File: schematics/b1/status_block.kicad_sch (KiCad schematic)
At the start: 42 parts, among them Q1 2N3904, Q2 2N3904, Q3 2N3904, Q4 2N3904, Q5 2N3904, Q6 2N3904, Q7 2N3904, Q8 2N3904, Q9 2N3904, SW9 SW_SPDT, U2 74HC595, U3 NE555P

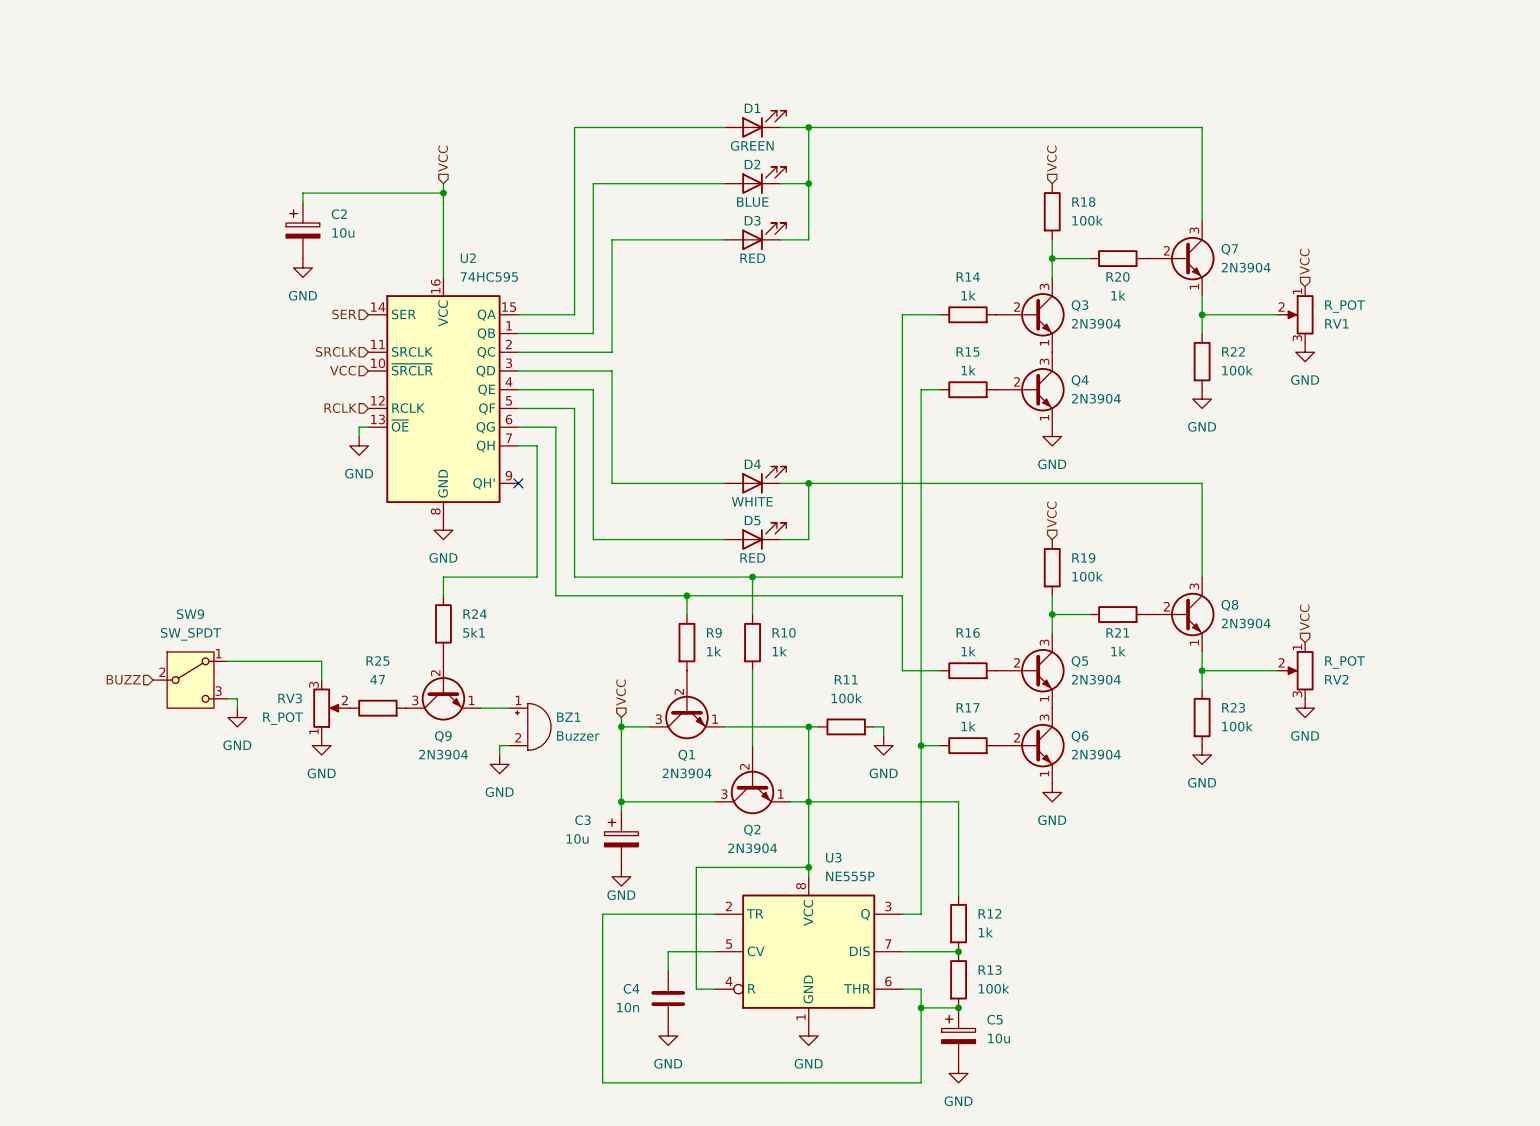
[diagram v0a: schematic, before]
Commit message: Added status block to the index page.
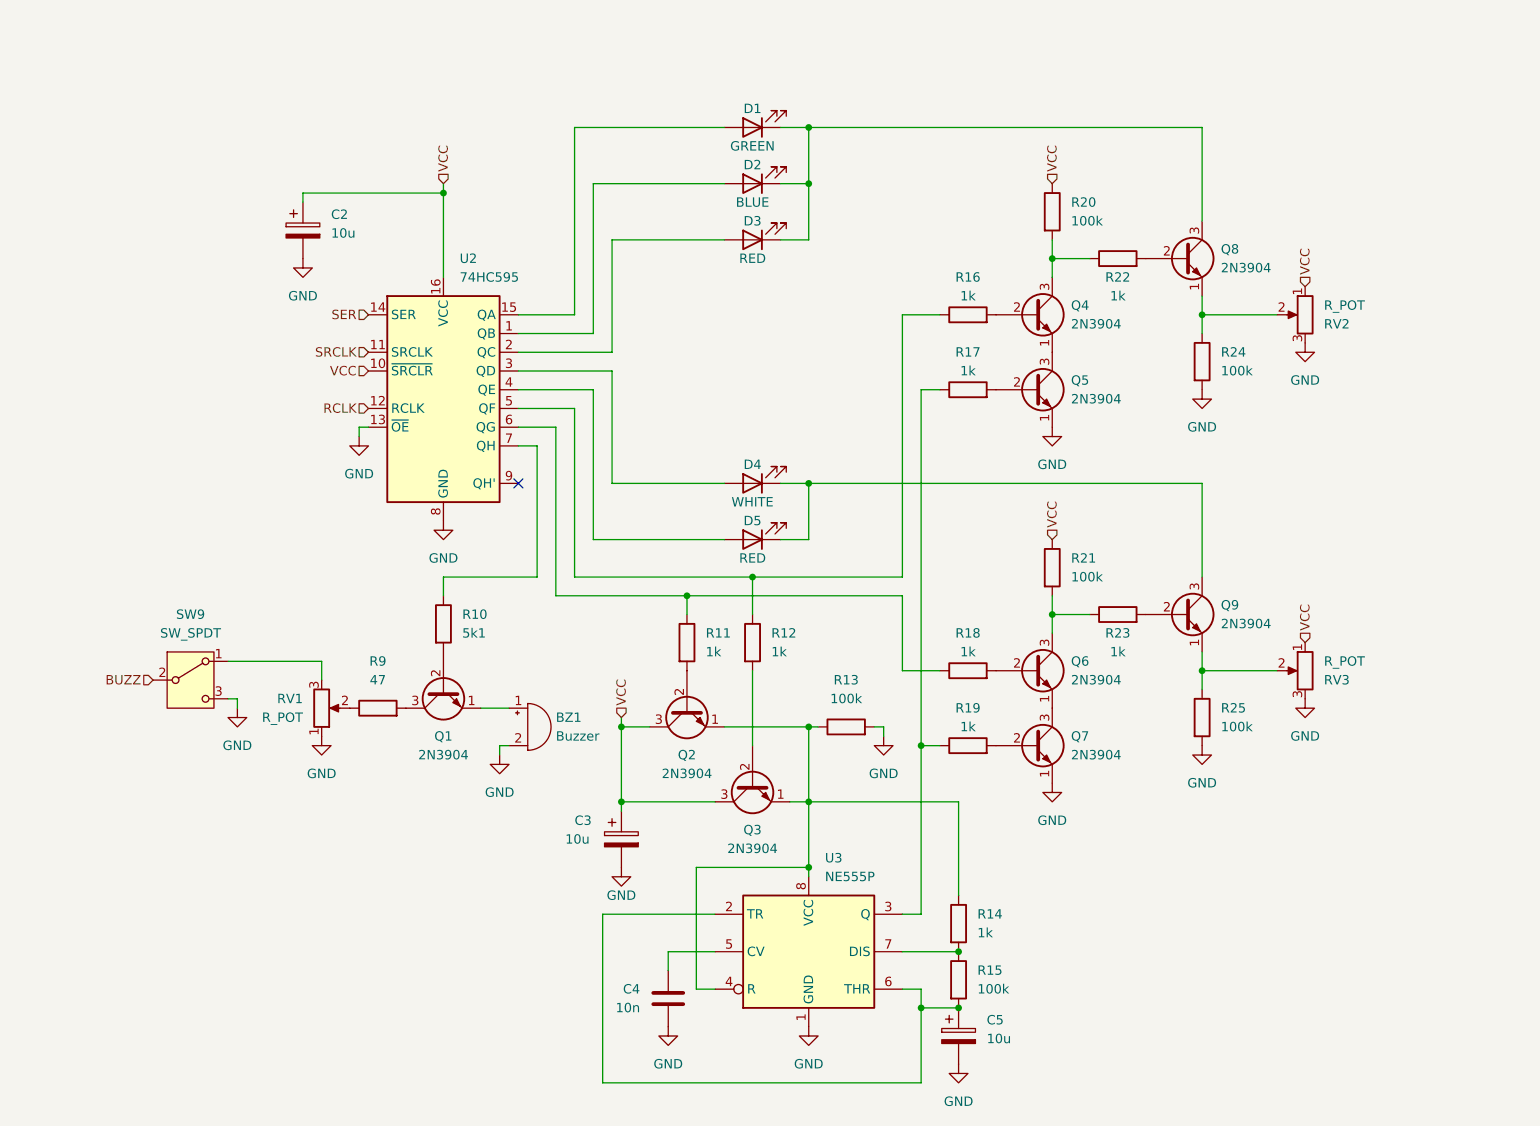
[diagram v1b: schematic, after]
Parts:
- renumbered Q9 to Q1, Q1 to Q2, Q2 to Q3, Q3 to Q4, Q4 to Q5, Q5 to Q6, Q6 to Q7, Q7 to Q8, Q8 to Q9, R24 to R10, R9 to R11, R10 to R12, R11 to R13, R12 to R14, R13 to R15, R14 to R16, R15 to R17, R16 to R18, R17 to R19, R18 to R20, R19 to R21, R20 to R22, R21 to R23, R22 to R24, R23 to R25, R25 to R9, RV3 to RV1, RV1 to RV2, RV2 to RV3

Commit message: Updated schematics.
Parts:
- added C7, C8: 0.1u, symbol Device:C
- C2, C3: value 10u -> 1u
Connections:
- net GND: now also C7.2, C8.2
- net VCC: now also C7.1, C8.1
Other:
- moved on the sheet: BZ1, C2, C3, C4, C5, D1, D2, D3, D4, D5, Q1, Q2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

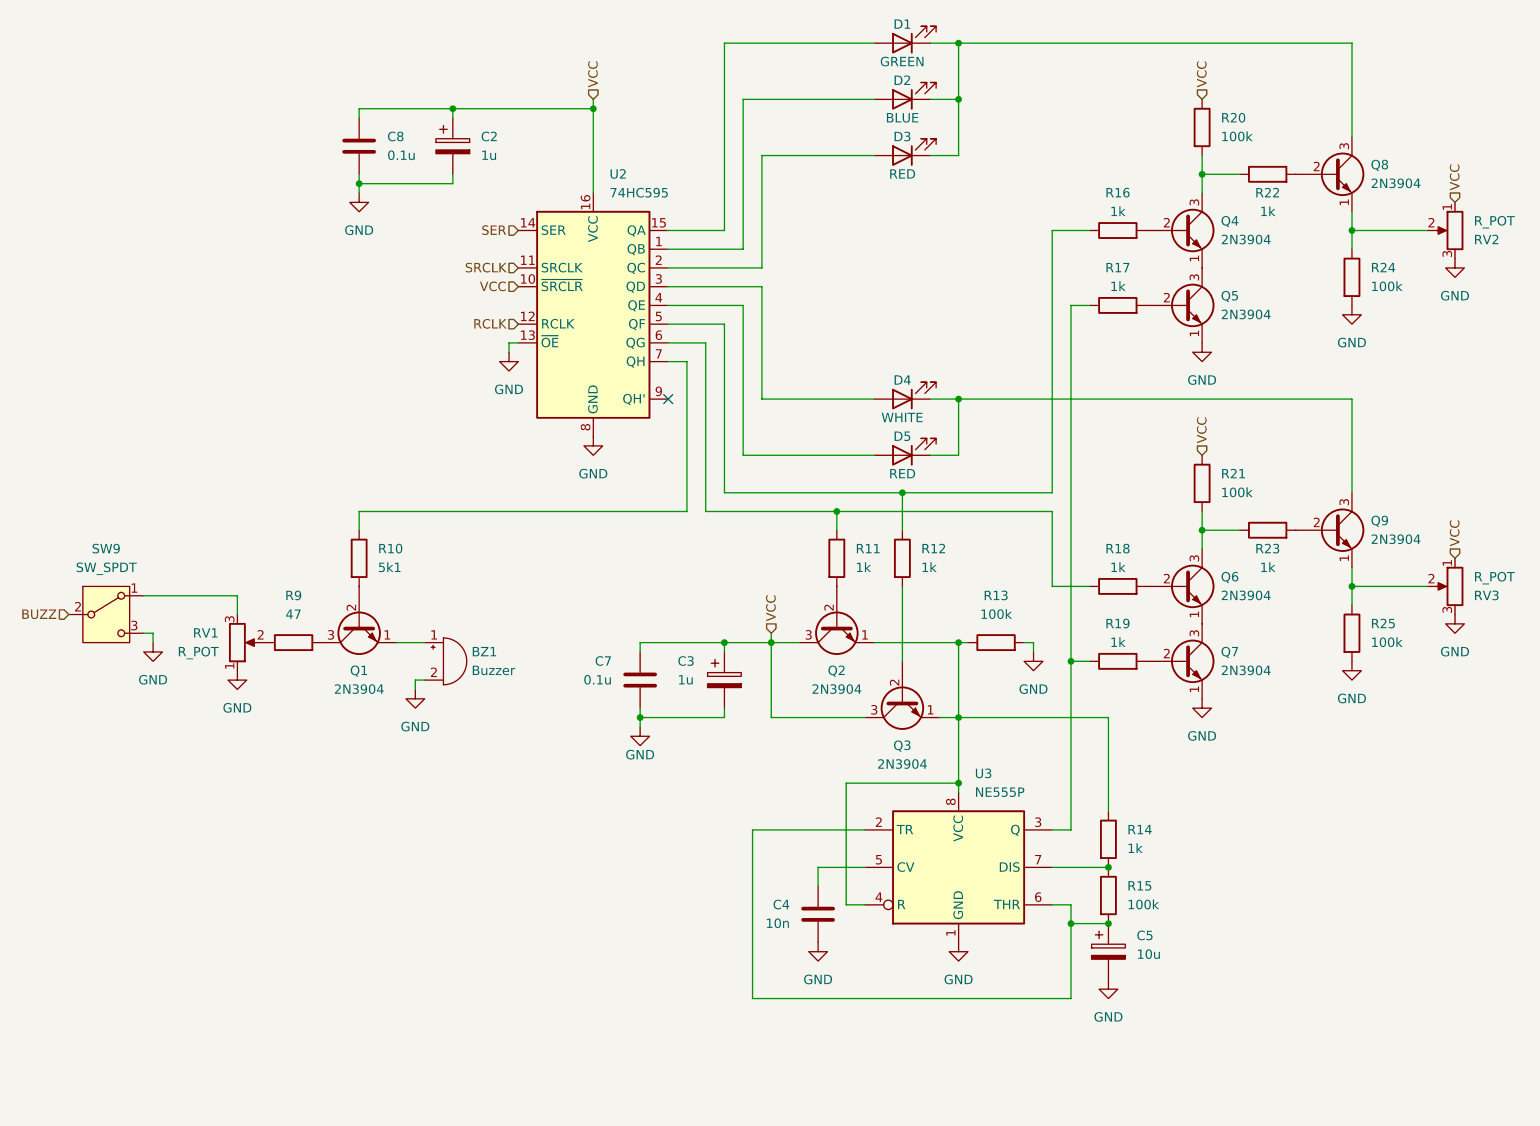
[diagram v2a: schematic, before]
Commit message: Updated bypass capacitor values.
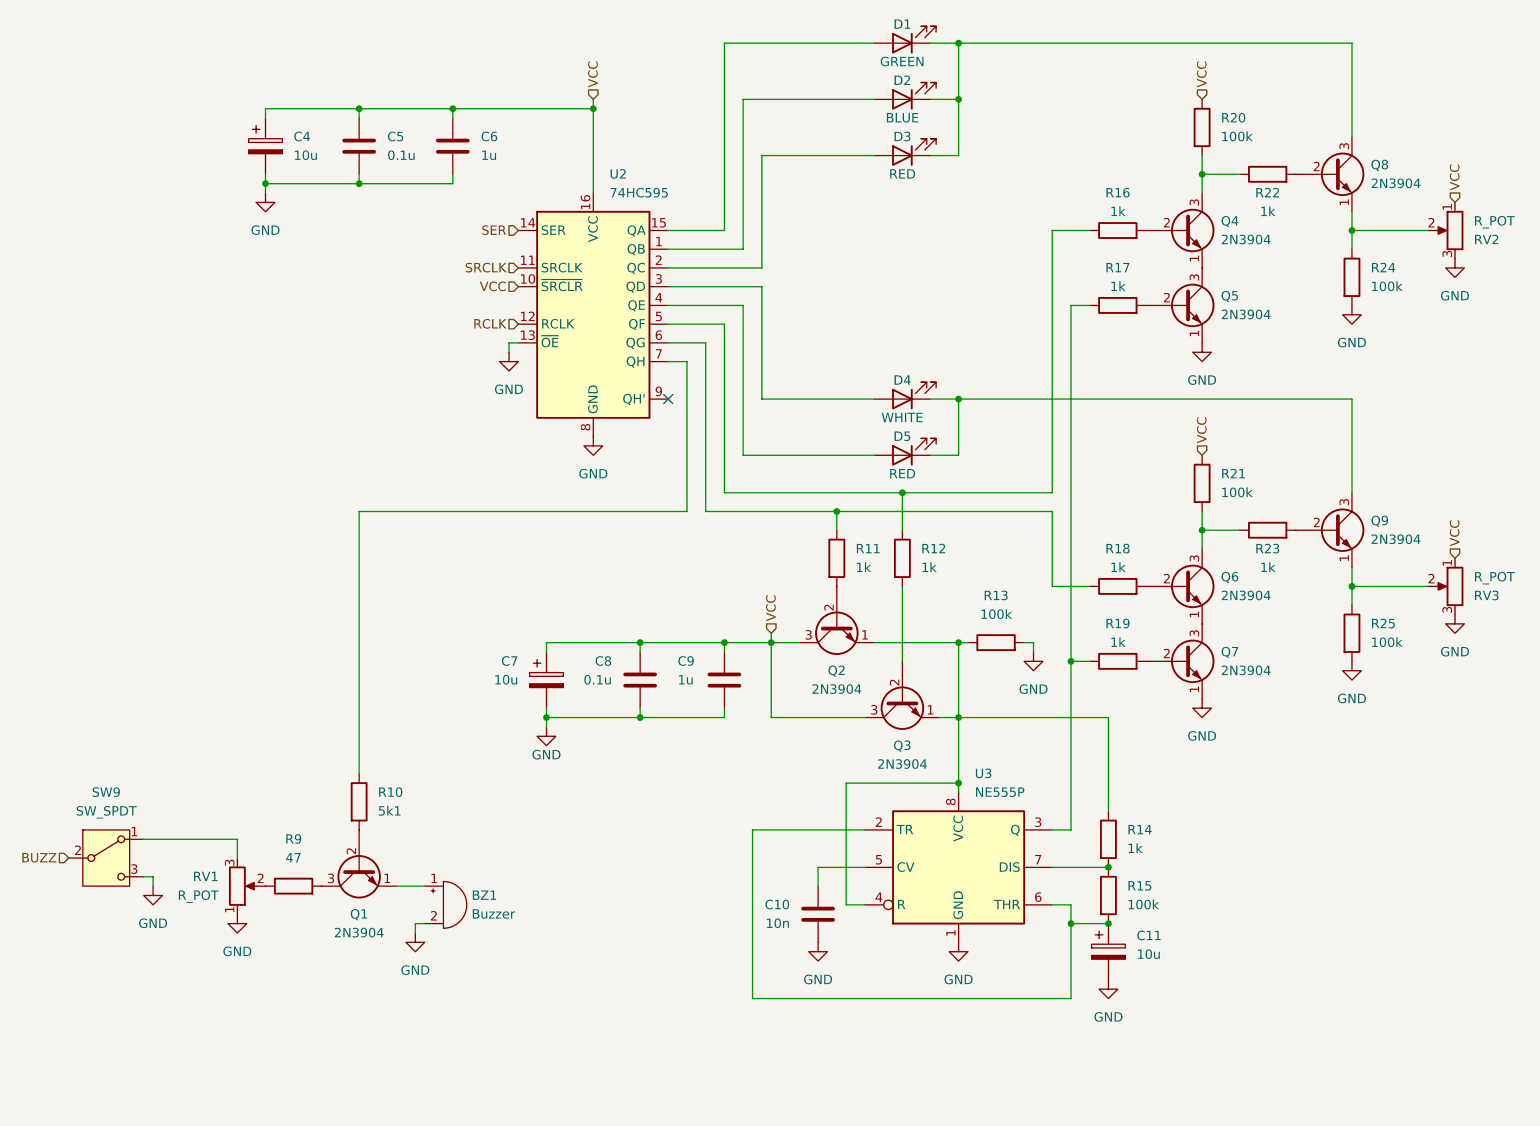
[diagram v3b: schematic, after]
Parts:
- added C4, C7: 10u, symbol Device:C_Polarized
- C6: renamed from C2; symbol Device:C_Polarized -> Device:C
- C9: renamed from C3; symbol Device:C_Polarized -> Device:C
- renumbered C4 to C10, C5 to C11, C8 to C5, C7 to C8
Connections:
- net GND: now also C4.2, C7.2
- net VCC: now also C4.1, C7.1
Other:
- moved on the sheet: BZ1, Q1, R10, R9, RV1, SW9

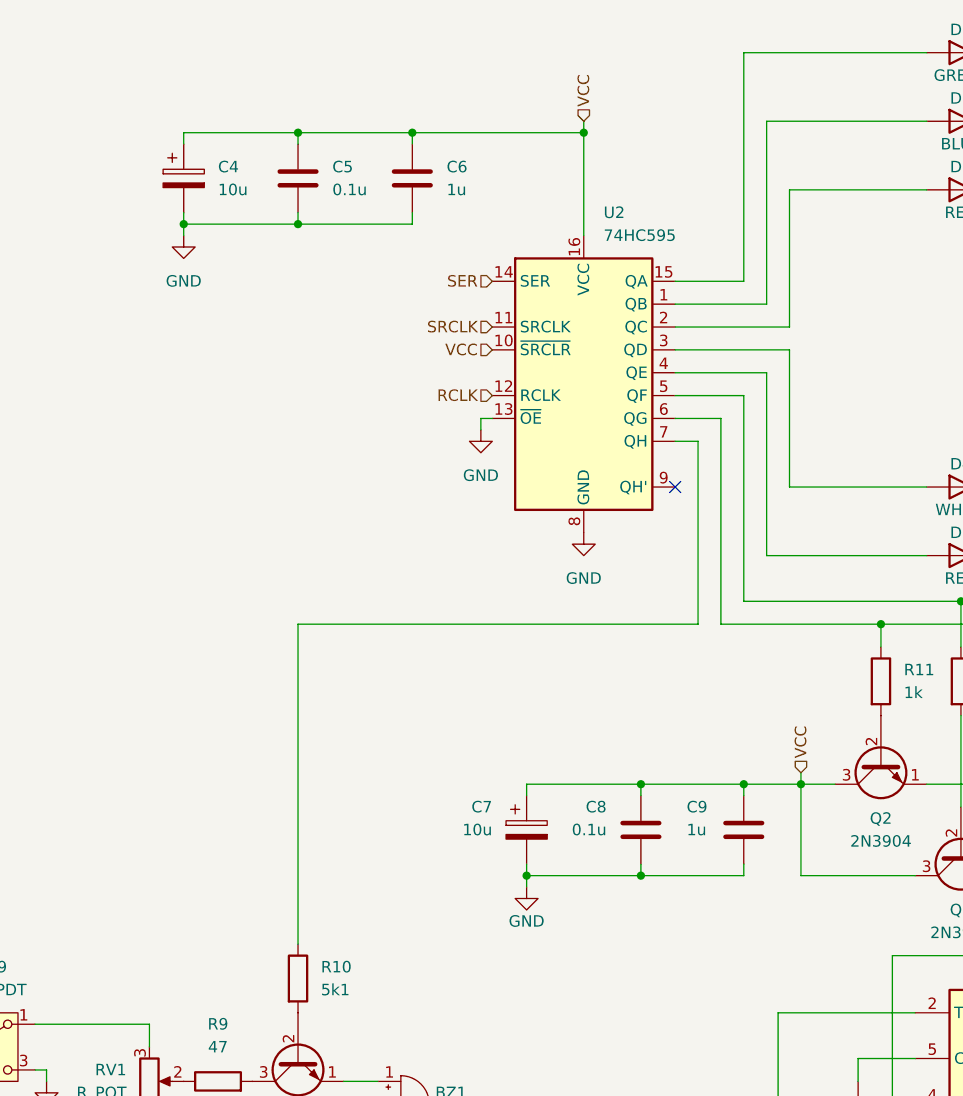
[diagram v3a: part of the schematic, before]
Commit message: Added schematic page for LoRa.
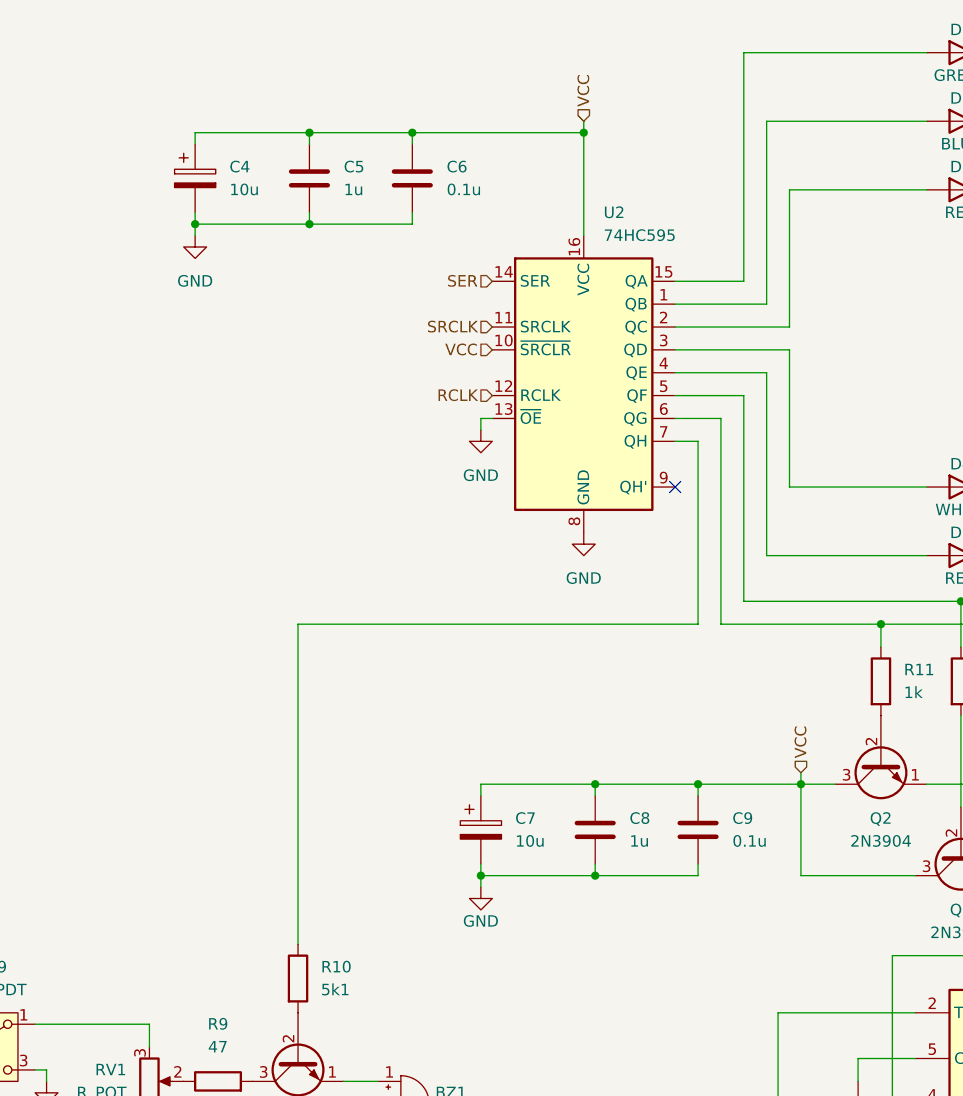
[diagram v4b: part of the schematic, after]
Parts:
- C5, C8: value 0.1u -> 1u
- C6, C9: value 1u -> 0.1u
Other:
- moved on the sheet: C4, C5, C7, C8, C9

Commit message: General schematic updates.
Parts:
- renumbered U2 to U3, U3 to U4
